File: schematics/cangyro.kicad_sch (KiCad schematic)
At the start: 14 parts, among them J1 Conn_01x06 CAN & PWR, J2 Conn_01x10 IMU BNO080, P1 USB_C_Plug_USB2.0 Serial, SW1 SW_Push IMU_RST, U1 STM32G474CBTx, U2 MCP2562-E-MF, U3 AP2112K-3.3

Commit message: Base software project
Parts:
- removed FB1, FB2: FerriteBead, Inductor_SMD:L_0805_2012Metric, symbol Device:FerriteBead
- removed J1: Conn_01x06 CAN & PWR, TerminalBlock_Phoenix:TerminalBlock_Phoenix_MKDS-1,5-6-5.08_1x06_P5.08mm_Horizontal, symbol Connector_Generic:Conn_01x06
- removed J2: Conn_01x10 IMU BNO080, Connector_PinSocket_1.00mm:PinSocket_1x10_P1.00mm_Vertical, symbol Connector_Generic:Conn_01x10
- removed P1: USB_C_Plug_USB2.0 Serial, Connector_USB:USB_C_Receptacle_HRO_TYPE-C-31-M-17, symbol Connector:USB_C_Plug_USB2.0
- removed R4: 5.1k Ohm, Resistor_SMD:R_0805_2012Metric, symbol Device:R
- removed U1: STM32G474CBTx, Package_QFP:LQFP-48_7x7mm_P0.5mm, symbol MCU_ST_STM32G4:STM32G474CBTx
- removed U2: MCP2562-E-MF, Package_DFN_QFN:DFN-8-1EP_3x3mm_P0.65mm_EP1.55x2.4mm, symbol Interface_CAN_LIN:MCP2562-E-MF
- removed U3: AP2112K-3.3, Package_TO_SOT_SMD:SOT-23-5, symbol Regulator_Linear:AP2112K-3.3
- added A1: RaspberryPi_Pico, Module:RaspberryPi_Pico_SMD_HandSolder, symbol MCU_Module:RaspberryPi_Pico_Debug
- added C1, C2: C, symbol Device:C
- added C3: 4.7nF, symbol Device:C
- added J1: Conn_01x10 IMU BNO080, symbol Connector_Generic:Conn_01x10
- added J2: Conn_01x06, symbol Connector_Generic:Conn_01x06
- added U2: MCP2515-xSO, Package_SO:SOIC-18W_7.5x11.6mm_P1.27mm, symbol Interface_CAN_LIN:MCP2515-xSO
- added U3: MCP2562-E-MF, Package_DFN_QFN:DFN-8-1EP_3x3mm_P0.65mm_EP1.55x2.4mm, symbol Interface_CAN_LIN:MCP2562-E-MF
- added Y1: Crystal, symbol Device:Crystal
- D1: footprint LED_SMD:LED_0805_2012Metric -> (none)
- R1: value 1k -> 10k; footprint Resistor_SMD:R_0805_2012Metric -> (none)
- R2: value 22Ohm -> 10k; footprint Resistor_SMD:R_0805_2012Metric -> (none)
- R3: value 22Ohm -> 300 Ohm; footprint Resistor_SMD:R_0805_2012Metric -> (none)
- SW1: value SW_Push IMU_RST -> SW_Push; footprint Button_Switch_SMD:SW_SPST_TL3342 -> (none)
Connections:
- net IMU_RST is gone; now on net GND: SW1.1
- net GND: now also A1.13 (GND), A1.18 (GND), A1.23 (GND), A1.28 (GND), A1.3 (GND), A1.33 (AGND), A1.38 (GND), A1.8 (GND), A1.D2 (GND), C1.1, C2.2, C3.2, J1.2 (Pin_2), J1.9 (Pin_9), J2.5 (Pin_5), U2.9 (VSS), U3.2 (VSS)
- net IMU_SCL: now also A1.22 (GPIO17), J1.3 (Pin_3)
- net IMU_SDA: now also A1.24 (GPIO18), J1.4 (Pin_4)
- net at R1.2: now also R2.2, R3.1, A1.36 (3V3), J1.1 (Pin_1), J1.10 (Pin_10), U3.5 (Vio); no longer D1.2 (A)
- net at R3.2: now also D1.2 (A)
- net at R2.1: now also SW1.2, A1.30 (RUN)
- net 3.3v: no longer names the net of R1.1
- net 3.3v: now also U3.8 (SHDN); no longer SW1.2
- new net: U2.1 (TXCAN), U3.1 (TXD)
- new net: U2.2 (RXCAN), U3.4 (RXD)
- new net: J2.1 (Pin_1), J2.3 (Pin_3), U3.6 (CANL)
- new net: J2.2 (Pin_2), J2.4 (Pin_4), U3.7 (CANH)
- new net: C3.1, U3.9 (PAD)
- new net: C1.2, U2.7 (OSC2), Y1.2
- new net: A1.20 (GPIO15), U2.12 (~{INT})
- new net: A1.7 (GPIO5), U2.13 (SCK)
- new net: A1.4 (GPIO2), U2.14 (SI)
- new net: A1.5 (GPIO3), U2.15 (SO)
- new net: A1.6 (GPIO4), U2.16 (~{CS})
- new net: C2.1, U2.8 (OSC1), Y1.1
- new net 5v: A1.39 (VSYS), J2.6 (Pin_6), U2.18 (VDD), U3.3 (VDD)
- no-connect marks 32 -> 34

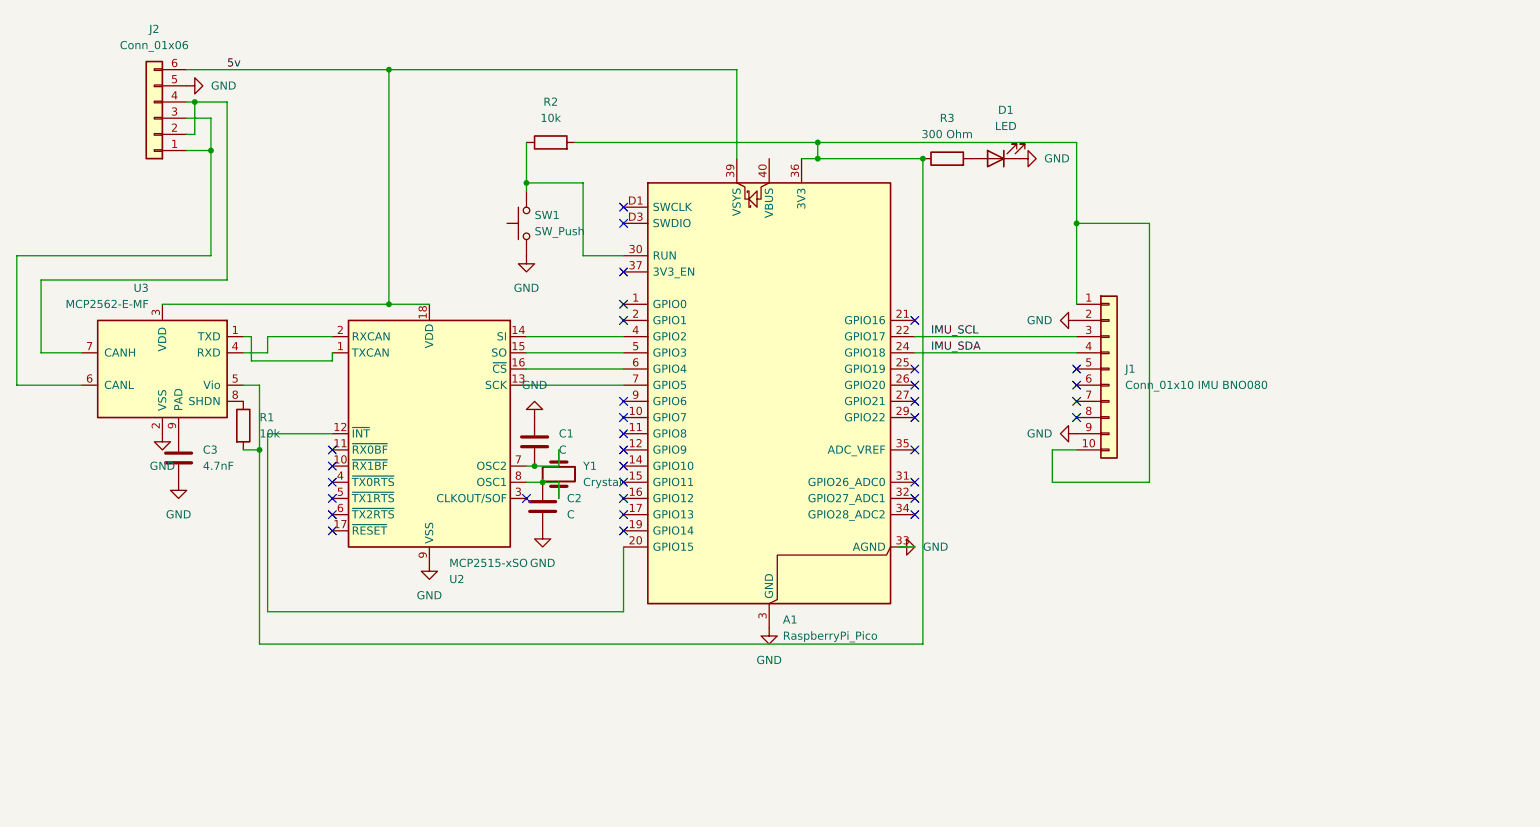
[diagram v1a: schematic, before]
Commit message: Replaced STM Microcontroller with PiPico, base code and new schematics
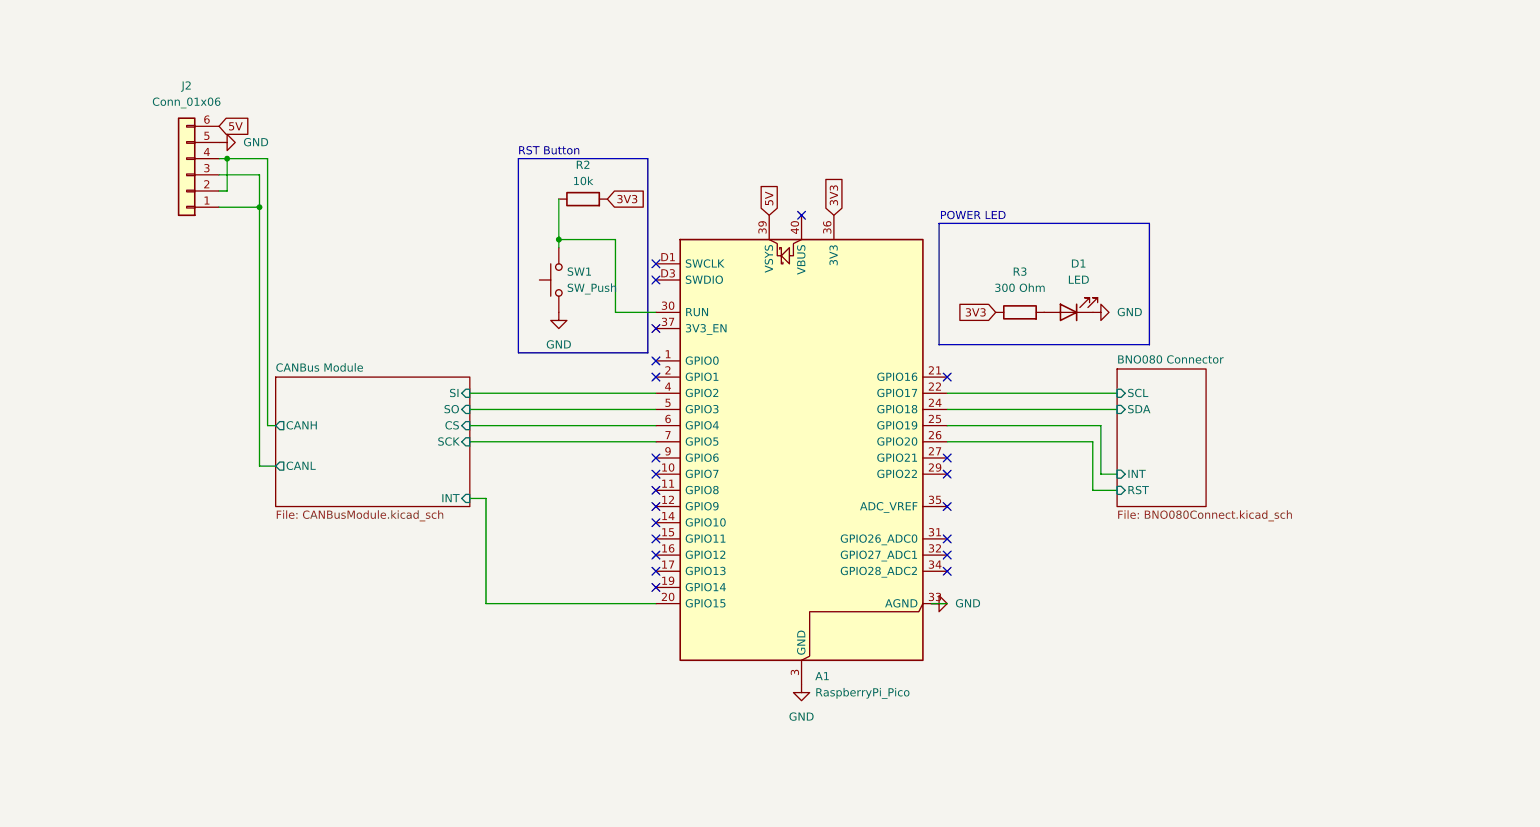
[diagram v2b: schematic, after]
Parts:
- removed C1, C2: C, symbol Device:C
- removed C3: 4.7nF, symbol Device:C
- removed J1: Conn_01x10 IMU BNO080, symbol Connector_Generic:Conn_01x10
- removed R1: 10k, symbol Device:R
- removed U2: MCP2515-xSO, Package_SO:SOIC-18W_7.5x11.6mm_P1.27mm, symbol Interface_CAN_LIN:MCP2515-xSO
- removed U3: MCP2562-E-MF, Package_DFN_QFN:DFN-8-1EP_3x3mm_P0.65mm_EP1.55x2.4mm, symbol Interface_CAN_LIN:MCP2562-E-MF
- removed Y1: Crystal, symbol Device:Crystal
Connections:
- net 3V3: now reaches A1.36 (3V3), R2.2, R3.1
- net CANBus Module/CANL: now reaches J2.1 (Pin_1), J2.3 (Pin_3)
- net CANBus Module/CANH: now reaches J2.2 (Pin_2), J2.4 (Pin_4)
- net CANBus Module/INT: now reaches A1.20 (GPIO15)
- net CANBus Module/SCK: now reaches A1.7 (GPIO5)
- net CANBus Module/SI: now reaches A1.4 (GPIO2)
- net CANBus Module/SO: now reaches A1.5 (GPIO3)
- net CANBus Module/CS: now reaches A1.6 (GPIO4)
- net BNO080 Connector/INT: now reaches A1.25 (GPIO19)
- net BNO080 Connector/RST: now reaches A1.26 (GPIO20)
- net 5v renamed 5V
- net IMU_SCL renamed BNO080 Connector/SCL
- net IMU_SDA renamed BNO080 Connector/SDA
- no-connect marks 34 -> 22
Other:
- added sheet BNO080 Connector (BNO080Connect.kicad_sch)
- added sheet CANBus Module (CANBusModule.kicad_sch)
- note added: "POWER LED"
- note added: "RST Button"
- moved on the sheet: A1, D1, J2, R2, R3, SW1
